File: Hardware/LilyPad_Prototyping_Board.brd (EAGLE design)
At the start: 109.2 x 82.5 mm, 196 parts, among them J1 SEWTAP_LONG-2SIDE, J10 SEWTAP_LONG-2SIDE, J11 SEWTAP_LONG-2SIDE, J12 SEWTAP_LONG-2SIDE, J13 SEWTAP_LONG-2SIDE, J14 SEWTAP_LONG-2SIDE, J15 AMP FCI 10103594-0001LF, J2 SEWTAP_LONG-2SIDE, J3 SEWTAP_LONG-2SIDE, J4 SEWTAP_LONG-2SIDE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

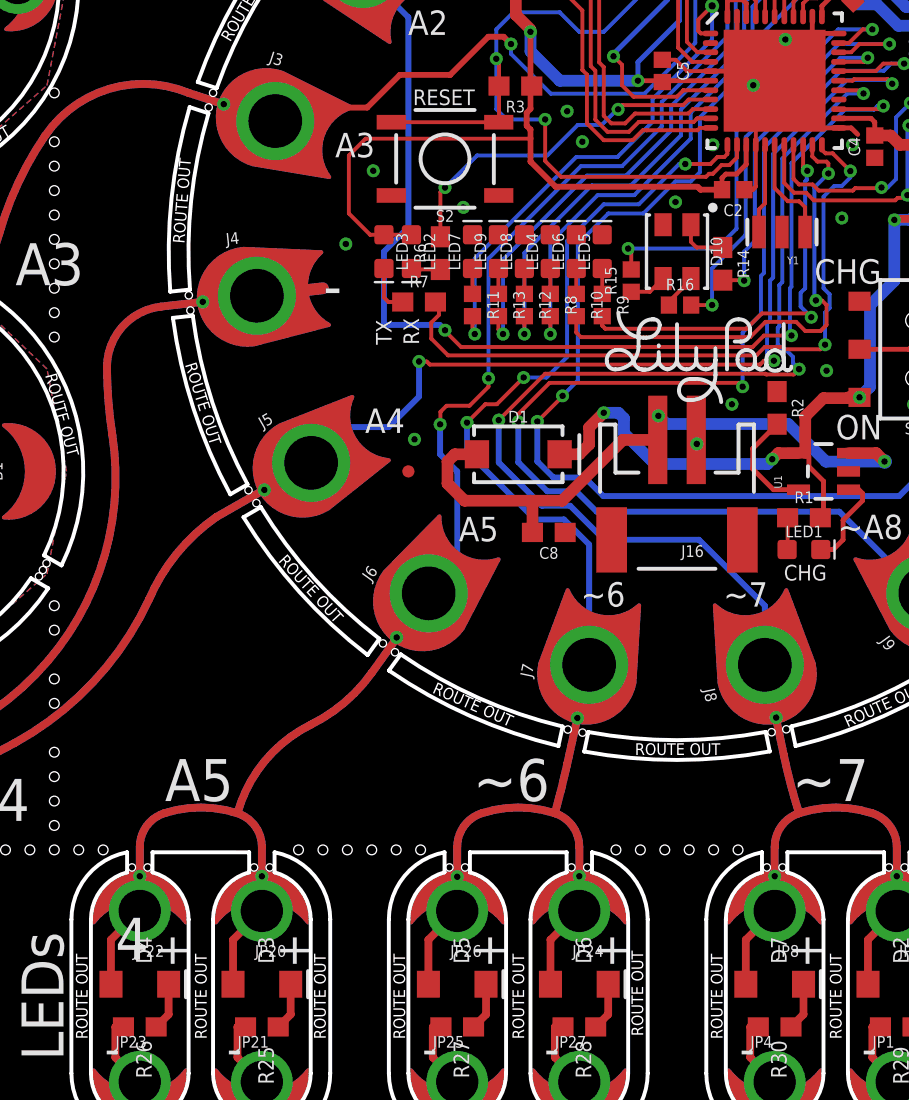
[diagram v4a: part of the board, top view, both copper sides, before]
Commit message: Moved lilypad logo to dodge connector, created v01 gerbers
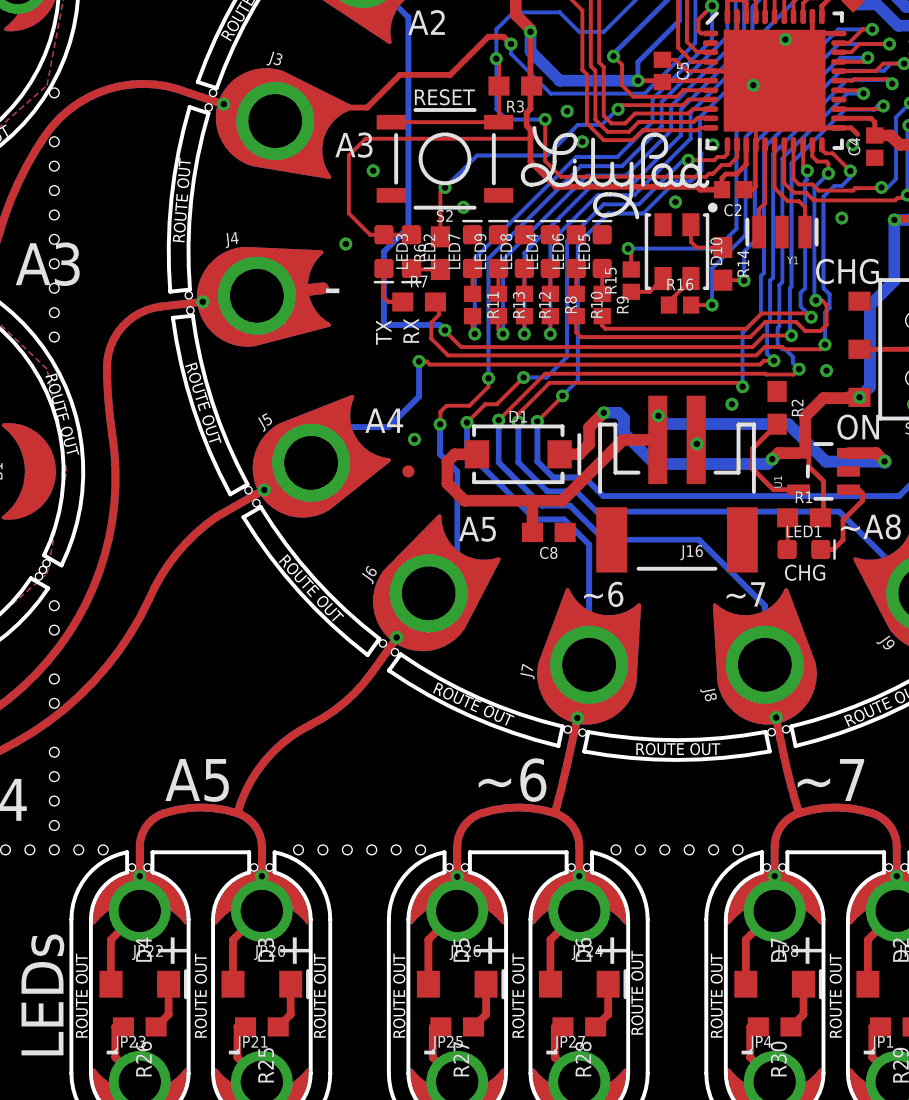
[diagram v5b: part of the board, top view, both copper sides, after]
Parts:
- moved U$13 10.6 mm to (-3.17, 4.45)
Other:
- board text removed: "4"
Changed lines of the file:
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@@
 <layer number="20" name="Dimension" color="6" fill="1" visible="yes" active="yes"/>
 <layer number="21" name="tPlace" color="16" fill="1" visible="yes" active="yes"/>
-<layer number="22" name="bPlace" color="14" fill="1" visible="yes" active="yes"/>
+<layer number="22" name="bPlace" color="14" fill="1" visible="no" active="yes"/>
 <layer number="23" name="tOrigins" color="15" fill="1" visible="yes" active="yes"/>
-<layer number="24" name="bOrigins" color="15" fill="1" visible="yes" active="yes"/>
+<layer number="24" name="bOrigins" color="15" fill="1" visible="no" active="yes"/>
 <layer number="25" name="tNames" color="7" fill="1" visible="no" active="yes"/>
 <layer number="26" name="bNames" color="7" fill="1" visible="no" active="yes"/>
 <layer number="27" name="tValues" color="7" fill="1" visible="no" active="yes"/>
 <layer number="28" name="bValues" color="7" fill="1" visible="no" active="yes"/>
-<layer number="29" name="tStop" color="7" fill="3" visible="no" active="yes"/>
+<layer number="29" name="tStop" color="7" fill="3" visible="yes" active="yes"/>
 <layer number="30" name="bStop" color="7" fill="6" visible="no" active="yes"/>
 <layer number="31" name="tCream" color="7" fill="4" visible="no" active="yes"/>
 <layer number="32" name="bCream" color="7" fill="5" visible="no" active="yes"/>
 <layer number="39" name="tKeepout" color="4" fill="11" visible="yes" active="yes"/>
-<layer number="40" name="bKeepout" color="1" fill="11" visible="yes" active="yes"/>
+<layer number="40" name="bKeepout" color="1" fill="11" visible="no" active="yes"/>
 <layer number="41" name="tRestrict" color="4" fill="10" visible="no" active="yes"/>
 <layer number="42" name="bRestrict" color="1" fill="10" visible="no" active="yes"/>
 <layer number="44" name="Drills" color="7" fill="1" visible="no" active="yes"/>
-<layer number="45" name="Holes" color="7" fill="1" visible="yes" active="yes"/>
+<layer number="45" name="Holes" color="7" fill="1" visible="no" active="yes"/>
 <layer number="46" name="Milling" color="3" fill="1" visible="no" active="yes"/>
 <layer number="51" name="tDocu" color="6" fill="1" visible="no" active="yes"/>
@@
 <text x="-10.5965625" y="-28.575" size="2.1844" layer="21" ratio="17">~6</text>
 <text x="-26.6303125" y="-28.575" size="2.1844" layer="21" ratio="17">A5</text>
-<text x="-29.21" y="-36.83" size="2.1844" layer="21" ratio="17">4</text>
 <text x="-34.4090625" y="-1.74625" size="2.1844" layer="21" ratio="17">A3</text>
 <text x="-29.1703125" y="13.3746875" size="2.1844" layer="21" ratio="17">A2</text>
@@
 <attribute name="PROD_ID" value="RES-12427" x="0.15875" y="-2.778125" size="1.778" layer="27" display="off"/>
 </element>
-<element name="U$13" library="newLilypadParts" package="LILYPAD-WEARABLES_LOGO-LILYPAD" value="LILYLOGO_SHORT" x="1.190625" y="-5.159375"/>
+<element name="U$13" library="newLilypadParts" package="LILYPAD-WEARABLES_LOGO-LILYPAD" value="LILYLOGO_SHORT" x="-3.175" y="4.445"/>
 <element name="U$35" library="LilyPad-Wearables" package="PETAL-SMALL-NOHOLE" value="SEWTAP-NOHOLE_SM_NH" x="-45.66" y="-4.93" rot="R210"/>
 <element name="U$36" library="LilyPad-Wearables" package="PETAL-SMALL-NOHOLE" value="SEWTAP-NOHOLE_SM_NH" x="-34.41" y="-11.43" rot="R90"/>
@@
 <wire x1="-7.381875" y1="-13.9303125" x2="-10.922" y2="-10.3901875" width="0.3048" layer="16"/>
 <wire x1="-10.922" y1="-10.3901875" x2="-10.922" y2="-8.89" width="0.3048" layer="16"/>
-<via x="0.428625" y="4.556125" extent="1-16" drill="0.3302"/>
-<wire x1="0.428625" y1="4.556125" x2="0.111125" y2="4.556125" width="0.2032" layer="16"/>
-<wire x1="0.111125" y1="4.556125" x2="-1.984375" y2="2.460625" width="0.2032" layer="16"/>
+<via x="0.587375" y="4.7545625" extent="1-16" drill="0.3302"/>
+<wire x1="0.587375" y1="4.7545625" x2="0.3095625" y2="4.7545625" width="0.2032" layer="16"/>
+<wire x1="0.3095625" y1="4.7545625" x2="-1.984375" y2="2.460625" width="0.2032" layer="16"/>
 <wire x1="-1.984375" y1="2.460625" x2="-3.81" y2="2.460625" width="0.2032" layer="16"/>
 <wire x1="-3.81" y1="2.460625" x2="-5.715" y2="0.555625" width="0.2032" layer="16"/>
@@
 <wire x1="2.622265625" y1="5.082890625" x2="2.460625" y2="4.92125" width="0.2032" layer="1"/>
 <wire x1="2.460625" y1="4.92125" x2="2.1034375" y2="4.92125" width="0.2032" layer="1"/>
-<wire x1="2.1034375" y1="4.92125" x2="1.7383125" y2="4.556125" width="0.2032" layer="1"/>
-<wire x1="1.7383125" y1="4.556125" x2="0.428625" y2="4.556125" width="0.2032" layer="1"/>
+<wire x1="2.1034375" y1="4.92125" x2="1.93675" y2="4.7545625" width="0.2032" layer="1"/>
+<wire x1="1.93675" y1="4.7545625" x2="0.587375" y2="4.7545625" width="0.2032" layer="1"/>
 <wire x1="-10.922" y1="-8.89" x2="-9.9695" y2="-7.9375" width="0.2032" layer="1"/>
 <wire x1="-9.9695" y1="-7.9375" x2="-9.36625" y2="-7.9375" width="0.2032" layer="1"/>
@@
 <wire x1="6.9215" y1="14.5415" x2="6.9215" y2="13.827125" width="0.2032" layer="16"/>
 <wire x1="6.9215" y1="13.827125" x2="4.365625" y2="11.27125" width="0.2032" layer="16"/>
-<wire x1="1.190625" y1="6.985" x2="1.190625" y2="4.1275" width="0.2032" layer="16"/>
-<wire x1="1.190625" y1="4.1275" x2="0.714375" y2="3.65125" width="0.2032" layer="16"/>
+<wire x1="1.190625" y1="6.985" x2="1.190625" y2="5.1990625" width="0.2032" layer="16"/>
+<wire x1="1.190625" y1="5.1990625" x2="1.27" y2="5.1196875" width="0.2032" layer="16"/>
+<wire x1="1.27" y1="5.1196875" x2="1.27" y2="4.206875" width="0.2032" layer="16"/>
+<wire x1="1.27" y1="4.206875" x2="0.714375" y2="3.65125" width="0.2032" layer="16"/>
 <wire x1="0.714375" y1="3.65125" x2="-0.079375" y2="3.65125" width="0.2032" layer="16"/>
 <wire x1="-0.079375" y1="3.65125" x2="-1.74625" y2="1.984375" width="0.2032" layer="16"/>

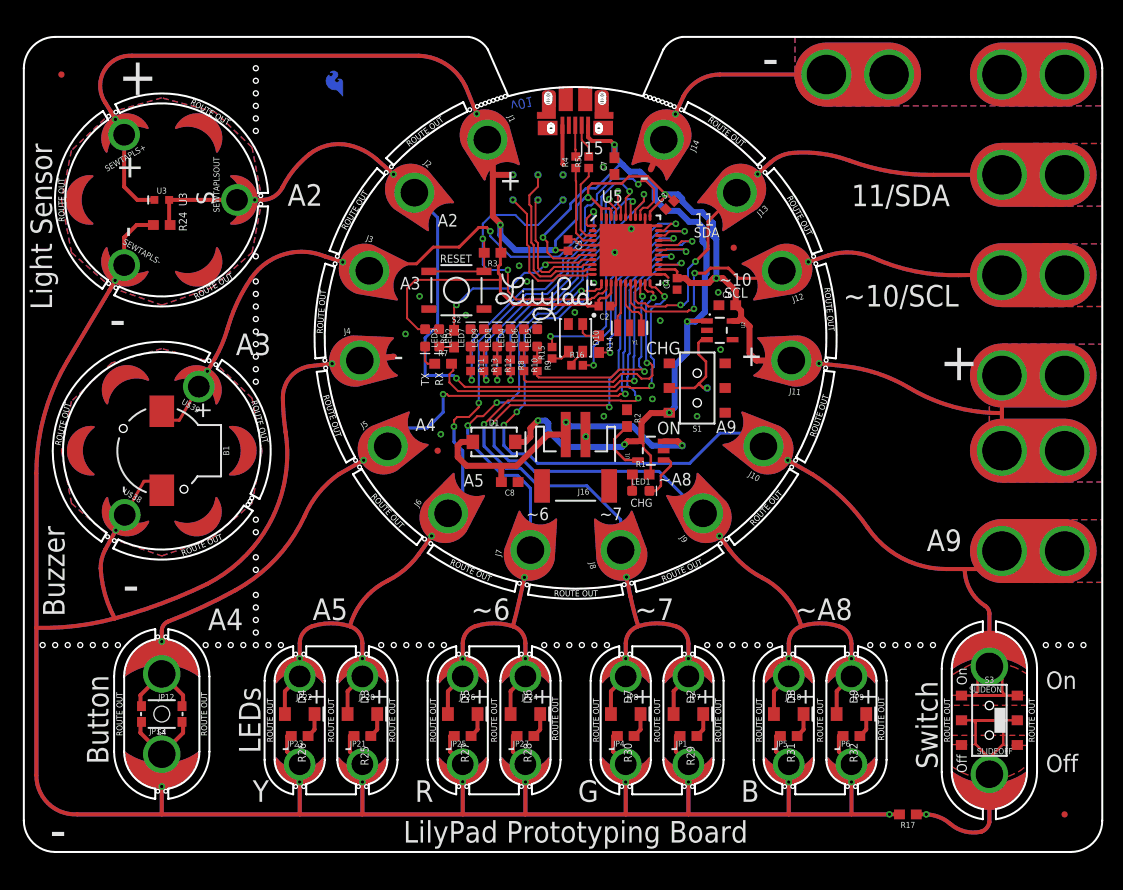
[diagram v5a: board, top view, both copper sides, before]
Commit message: Adjusted routes, drills, and USB connector for PCB fab house requirements, incremented design to v03
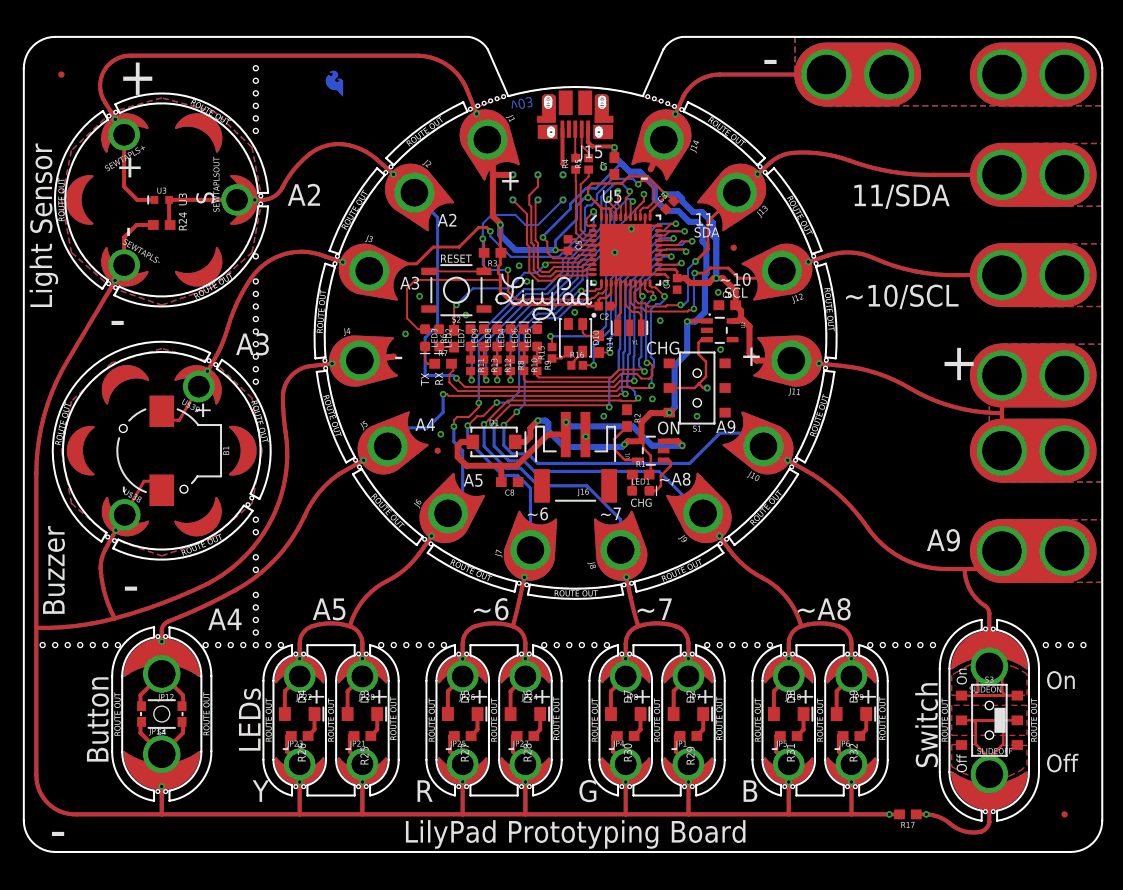
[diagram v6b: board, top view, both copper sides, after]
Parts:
- moved J15 0.40 mm to (0.00, 22.5)
- moved R4 0.16 mm to (0.02, 17.6)
- moved R5 0.16 mm to (1.33, 17.6)
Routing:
- net VCC_1: track 86.1 -> 85.5 mm
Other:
- outline, holes or cut-outs redrawn
- board text added: "v03"
- board text removed: "v01"

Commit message: Implemented most physical changes from proto 1
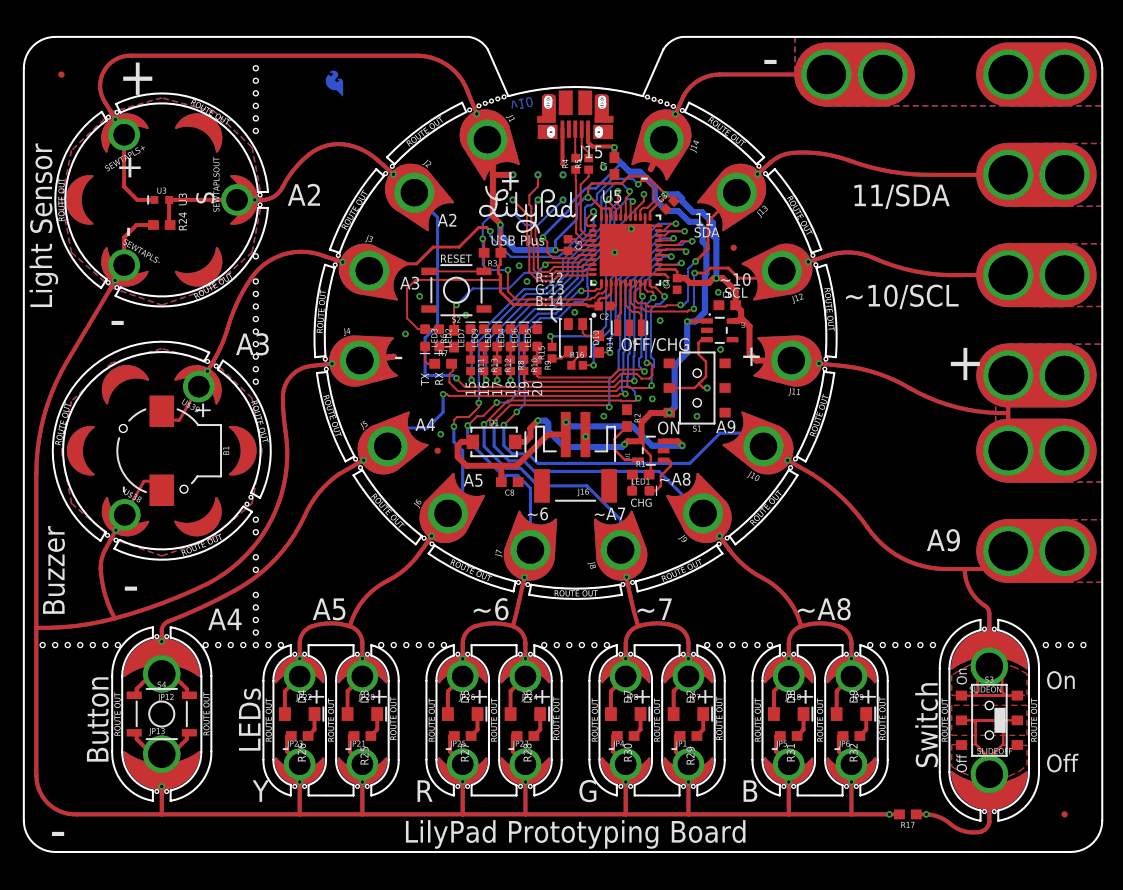
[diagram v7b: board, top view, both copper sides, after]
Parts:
- S4: value MOMENTARY-SWITCH-SPST-SMD-4.6X2.8MM -> MOMENTARY-SWITCH-SPST-SMD-5.2-REDUNDANT; device SparkFun-Switches:TACTILE_SWITCH_SMD_4.6X2.8MM -> SparkFun-Switches:TACTILE_SWITCH_SMD_5.2MM
- moved U$13 9.02 mm to (-4.82, 13.3)
- moved U$1 2.34 mm to (0.00, 2.18)
- moved U$41 0.63 mm to (43.8, -11.4)
- moved U$42 0.63 mm to (43.8, -3.81)
- moved U$51/SDA 0.63 mm to (43.8, 16.5)
- moved U$52/SCL 0.63 mm to (43.8, 6.35)
- moved U$52/SCL1 0.63 mm to (43.8, -21.6)
- moved U$54 0.63 mm to (43.8, 26.7)
- turned S4 to 0 degrees
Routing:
- net GND: track 637.2 -> 636.6 mm
- net D4: track 131.4 -> 130.9 mm
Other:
- outline, holes or cut-outs redrawn
- board text added: "15"
- board text added: "16"
- board text added: "17"
- board text added: "18"
- board text added: "19"
- board text added: "20"
- board text added: "B:14"
- board text added: "G:13"
- board text added: "OFF/CHG"
- board text added: "R:12"
- board text added: "USB Plus"
- board text added: "v10"
- board text added: "~A7"
- board text removed: "v03"

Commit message: More proto changes in
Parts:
- removed U$43, U$72: LILYLOGO_ABR, newLilypadParts:LILYPAD-WEARABLES_LOGO-L
- added U$5, U$6: LILYLOGO_SHORT, newLilypadParts:LILYPAD-WEARABLES_LOGO-LILYPAD
- LED2: value RED -> Yellow
- LED3: value RED -> GREEN
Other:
- board text removed: "~7"
